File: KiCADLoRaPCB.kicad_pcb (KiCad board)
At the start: 2 copper layers, 114.8 x 85.1 mm, 13 parts, among them J1 Raspberry_Pi_2_3, J2 RHF-GW, J3 Jack-DC

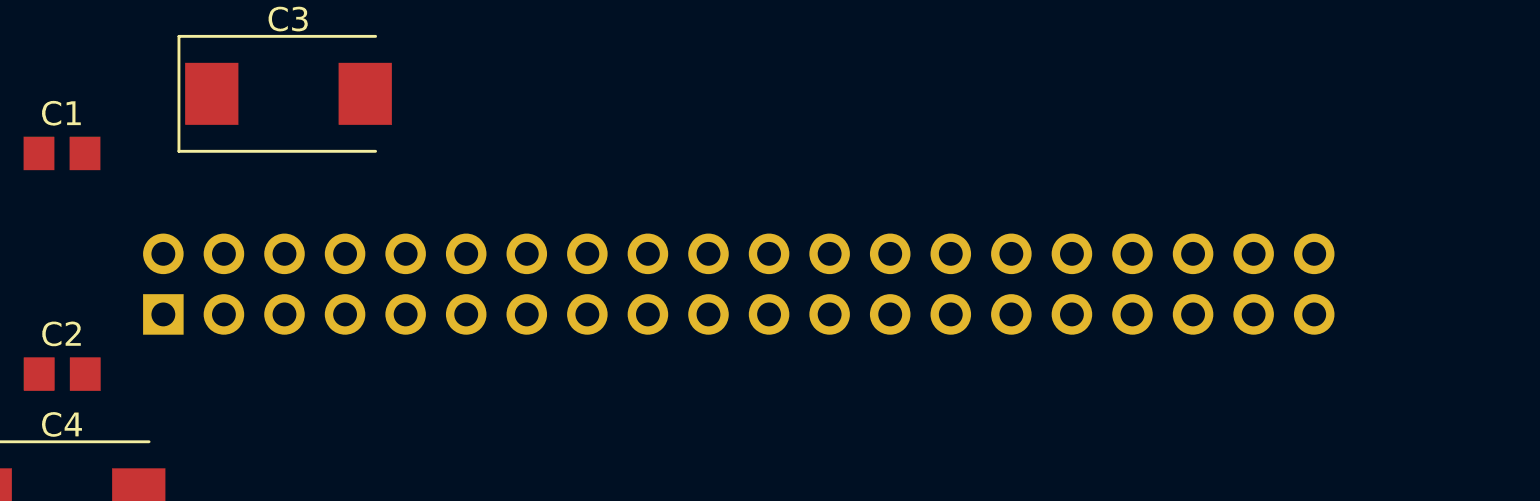
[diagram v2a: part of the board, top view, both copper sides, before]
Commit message: aligned the gpio pin header
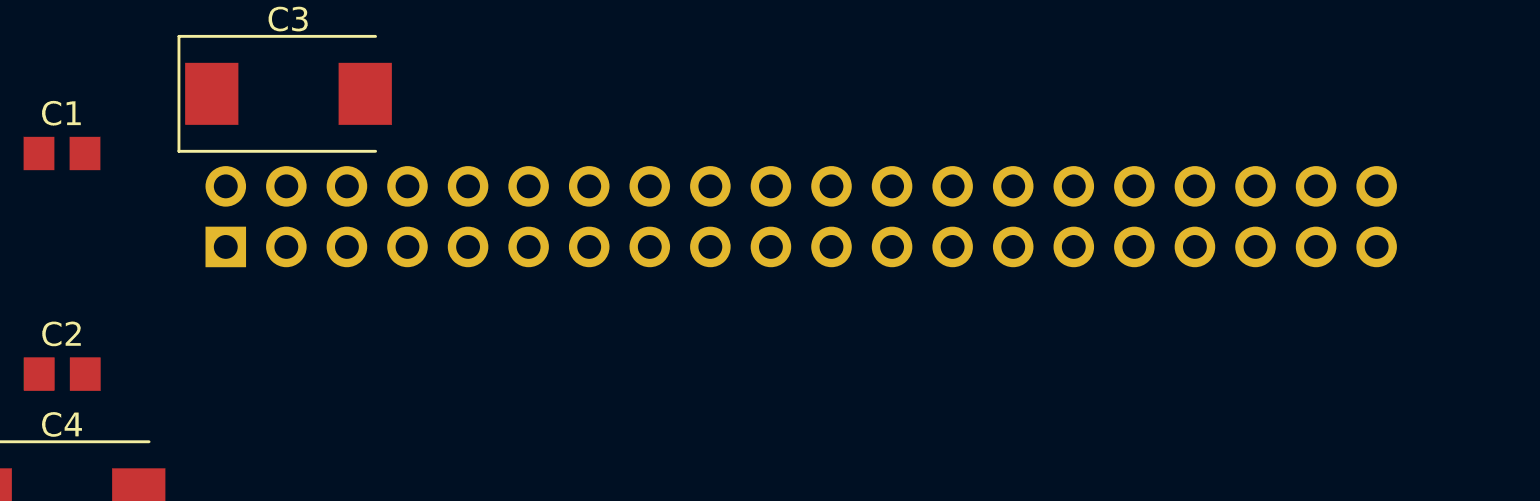
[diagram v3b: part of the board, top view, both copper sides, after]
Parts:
- moved J1 3.86 mm to (86.9, 58.4)
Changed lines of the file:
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@@
     (area 60.884999 45.644999 175.843001 130.885001)
     (thickness 1.6)
-    (drawings 2956)
+    (drawings 2957)
     (tracks 0)
     (zones 0)
@@
     (38 B.Mask user)
     (39 F.Mask user)
-    (40 Dwgs.User user)
+    (40 Dwgs.User user hide)
     (41 Cmts.User user)
     (42 Eco1.User user)
@@
   )
   (module Connector_PinSocket_2.54mm:PinSocket_2x20_P2.54mm_Vertical (layer B.Cu)
-    (at 84.25 61.25 270)
+    (at 86.868 58.42 270)
     (descr "Through hole straight socket strip, 2x20, 2.54mm pitch, double cols (from Kicad 4.0.7), script generated")
     (tags "Through hole socket strip THT 2x20 2.54mm double row")
@@
     (pad 1 np_thru_hole circle (at 0 0) (size 4.3 4.3) (drill 4.3) (layers *.Cu *.Mask))
   )
+  (dimension 12.954 (width 0.3) (layer Margin)
+    (gr_text "12.954 mm" (at 79.121 43.608) (layer Margin)
+      (effects (font (size 1.5 1.5) (thickness 0.3)))
+    )
+    (feature1 (pts (xy 85.598 57.15) (xy 85.598 42.258)))
+    (feature2 (pts (xy 72.644 57.15) (xy 72.644 42.258)))
+    (crossbar (pts (xy 72.644 44.958) (xy 85.598 44.958)))
+    (arrow1a (pts (xy 85.598 44.958) (xy 84.471496 45.544421)))
+    (arrow1b (pts (xy 85.598 44.958) (xy 84.471496 44.371579)))
+    (arrow2a (pts (xy 72.644 44.958) (xy 73.770504 45.544421)))
+    (arrow2b (pts (xy 72.644 44.958) (xy 73.770504 44.371579)))
+  )
   (gr_line (start 67.564 119.38) (end 67.818 119.38) (angle 90) (layer Eco2.User) (width 0.2))

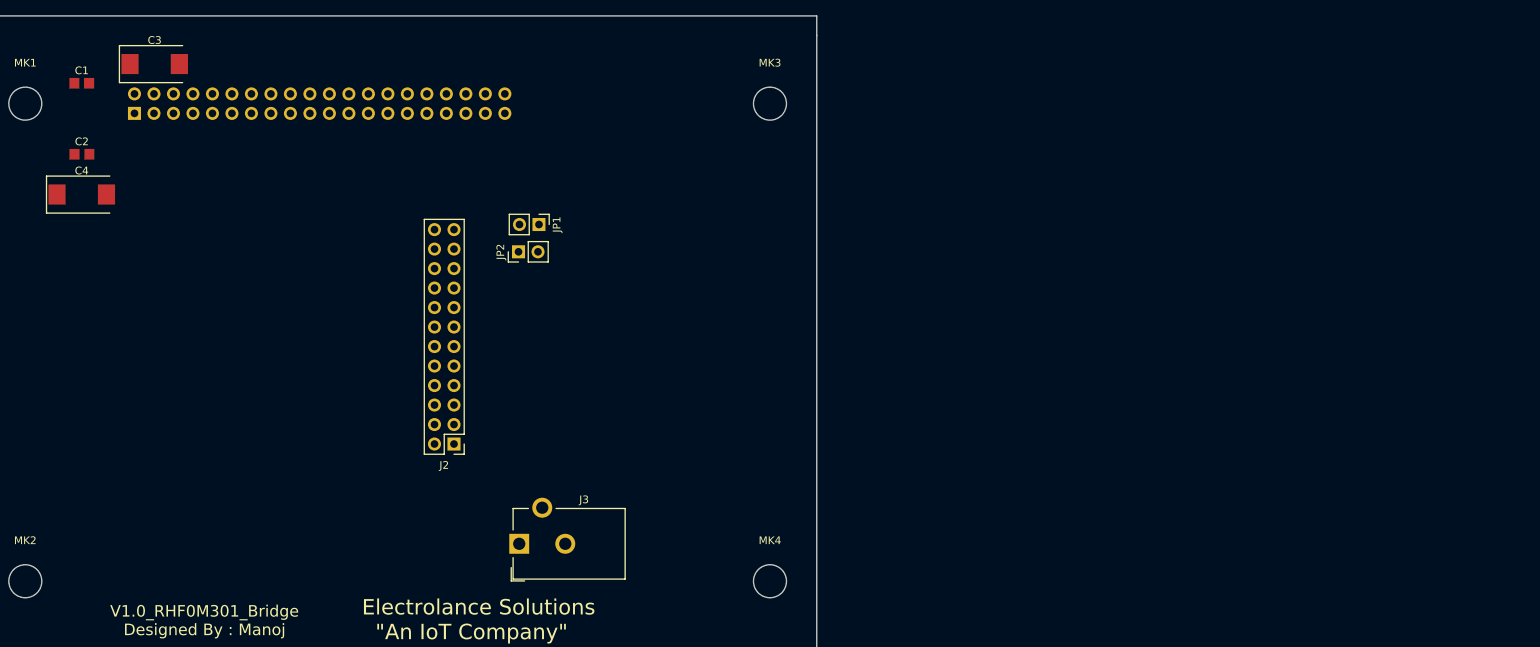
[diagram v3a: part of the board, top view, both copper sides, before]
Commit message: RisingHF board outline drawed on Cmts.User layer
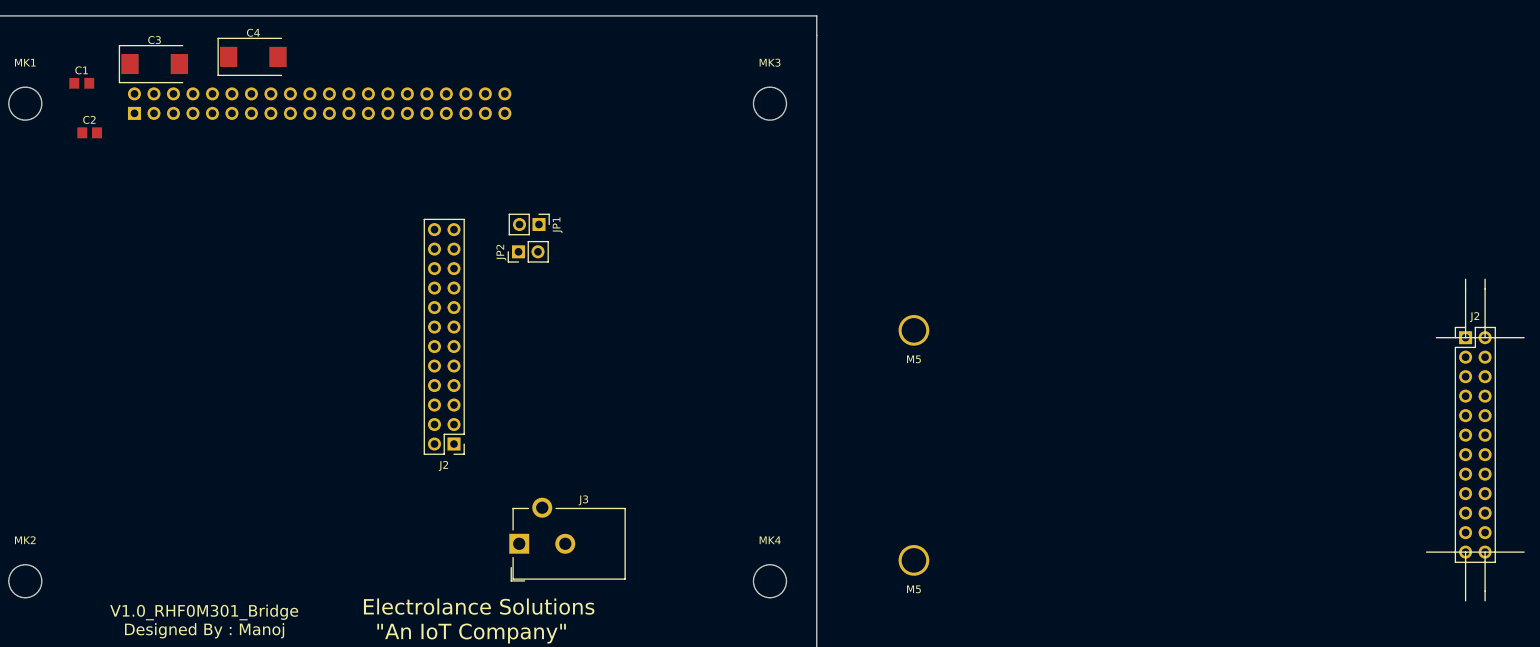
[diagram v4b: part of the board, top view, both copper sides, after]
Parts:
- added J2: RHF-GW, Connector_PinSocket_2.54mm:PinSocket_2x12_P2.54mm_Vertical, F.Cu at (260.3, 87.6)
- added M5: 3.2mm, MountingHole:MountingHole_3.2mm_M3_DIN965_Pad, F.Cu at (188.4, 86.7)
- added M5: 3.2mm, MountingHole:MountingHole_3.2mm_M3_DIN965_Pad, F.Cu at (188.4, 116.7)
- moved C4 28.7 mm to (102.4, 51.1)
- moved C2 2.97 mm to (81.0, 61.0)

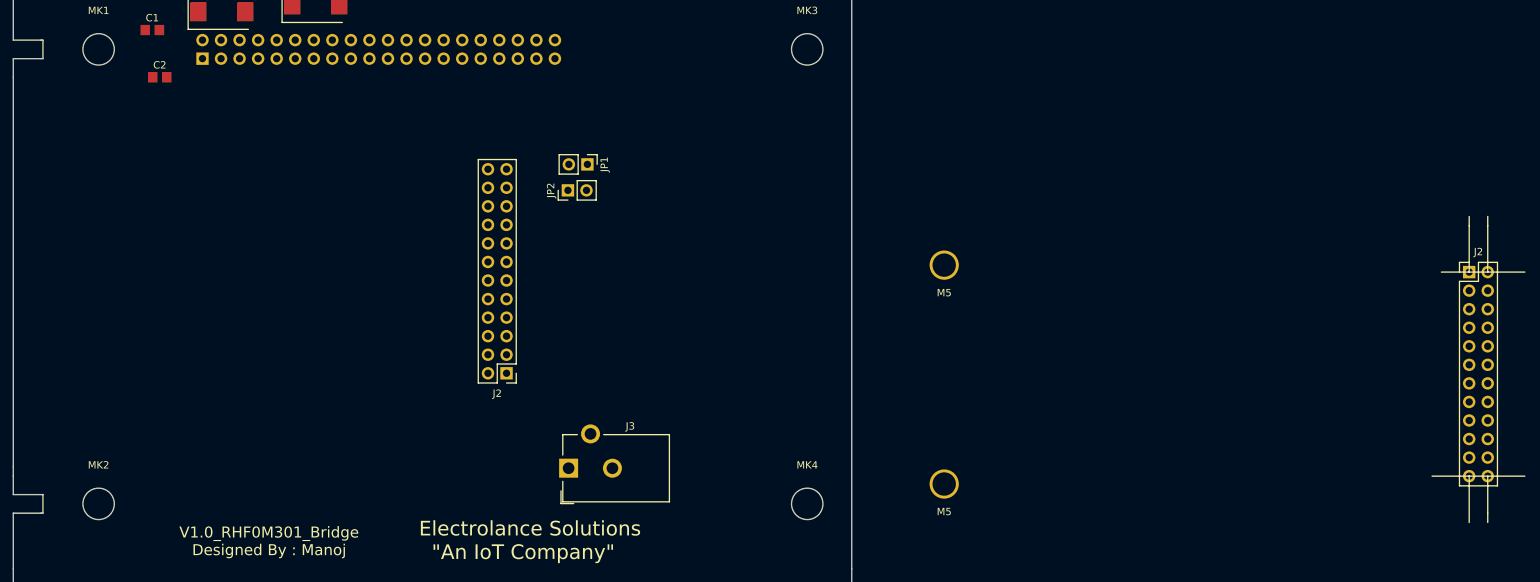
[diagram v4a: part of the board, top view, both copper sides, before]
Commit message: header risingHF pin aligned
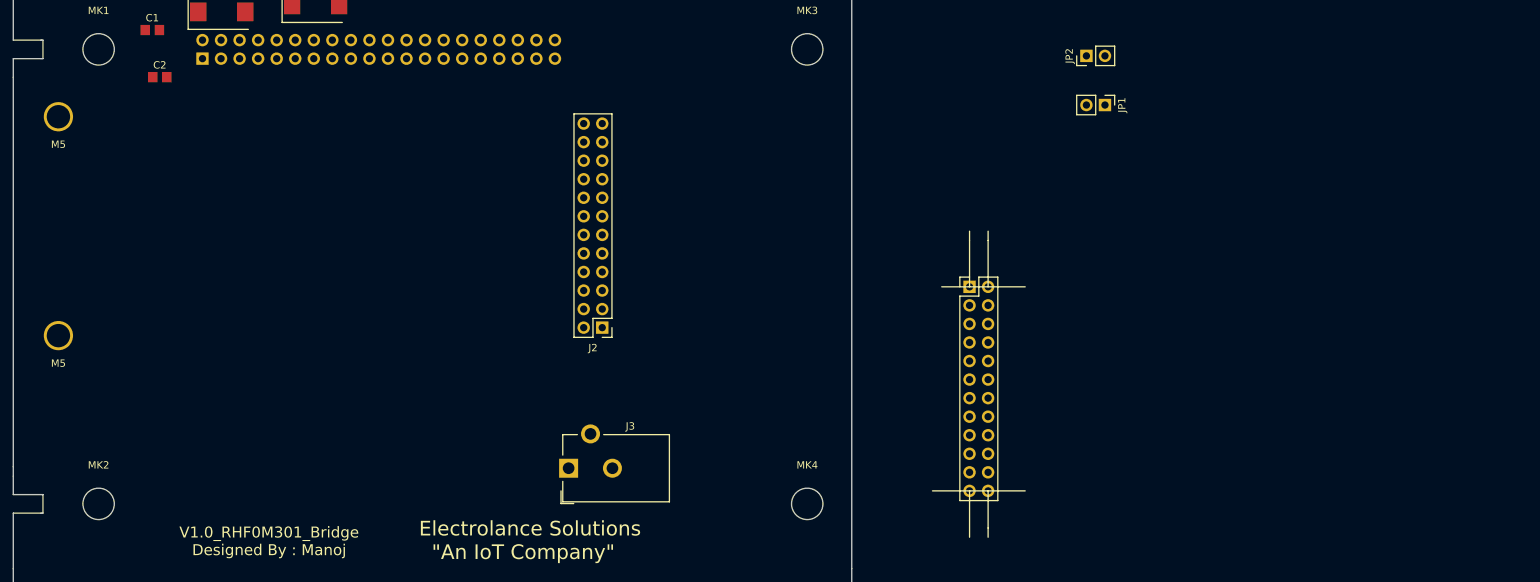
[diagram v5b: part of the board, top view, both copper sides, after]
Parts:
- moved M5 123.0 mm to (67.1, 66.4)
- moved M5 123.0 mm to (67.1, 96.3)
- moved JP2 73.3 mm to (207.9, 58.0)
- moved JP1 71.3 mm to (210.4, 64.8)
- moved J2 68.4 mm to (191.9, 89.7)
- moved J2 14.5 mm to (141.6, 95.2)

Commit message: PCB done but need advise on POWER Trace
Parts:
- removed the J2 at (191.9, 89.7)
- added J9: RHF-GWx, Connector_PinSocket_2.54mm:PinSocket_2x12_P2.54mm_Vertical, F.Cu at (353.1, 61.5)
- moved JP2 96.5 mm to (129.5, 114.3)
- moved JP1 87.4 mm to (128.0, 94.0)
- moved C1 76.5 mm to (142.2, 99.1), turned to 270 degrees
- moved C2 69.1 mm to (138.7, 99.1), turned to 270 degrees
- moved C3 66.7 mm to (134.6, 101.1), turned to 270 degrees
- moved C4 56.7 mm to (129.0, 101.1), turned to 270 degrees
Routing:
- net /5VR: track 0.00 -> 65.6 mm
- net Net-(J1-Pad26): track 0.00 -> 57.6 mm
- net +5V: track 0.00 -> 48.1 mm
- net Net-(J1-Pad21): track 0.00 -> 41.2 mm
- net Net-(J1-Pad24): track 0.00 -> 36.7 mm
- net Net-(J1-Pad19): track 0.00 -> 36.2 mm
- net Net-(J1-Pad23): track 0.00 -> 32.1 mm
- net GND: track 0.00 -> 26.3 mm, vias 0 -> 1
- net Net-(J3-Pad1): track 0.00 -> 5.00 mm
- added copper zone on F.Cu, net +5V
- added copper zone on B.Cu, net GND
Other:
- net class SPI added: clearance 0.518, trace_width 0.25, via_dia 0.6, via_drill 0.4
